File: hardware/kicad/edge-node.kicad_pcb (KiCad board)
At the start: 4 copper layers, 140 x 70 mm, 0 parts

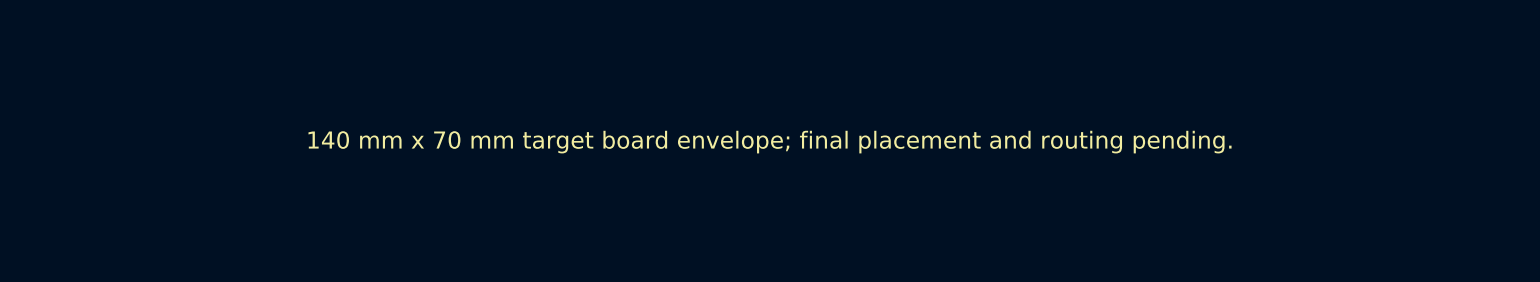
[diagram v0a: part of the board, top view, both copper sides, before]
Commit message: Add smartphone-first prototype and hosted backend
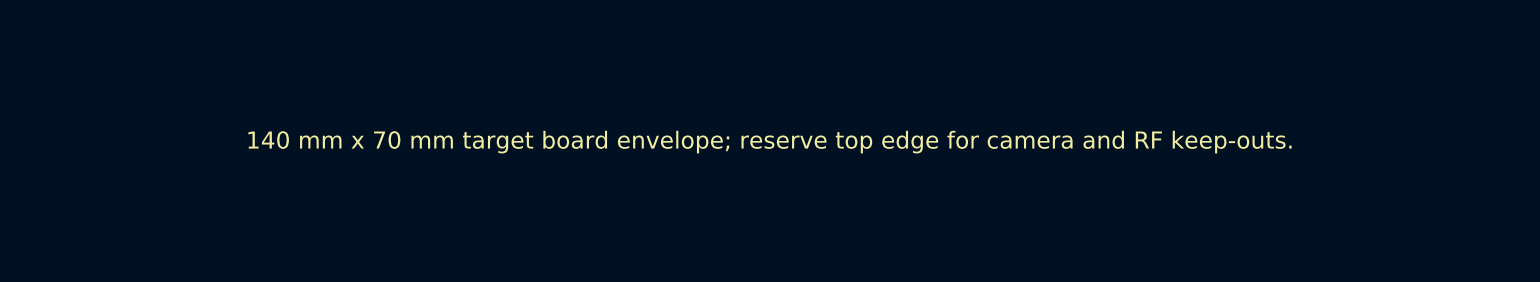
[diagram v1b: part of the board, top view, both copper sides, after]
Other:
- board text added: "140 mm x 70 mm target board envelope; reserve top edge for camera and RF keep-outs."
- board text removed: "140 mm x 70 mm target board envelope; final placement and routing pending."
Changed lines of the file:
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@@
   )
   (gr_rect (start 0 0) (end 140 70) (stroke (width 0.1) (type default)) (fill none) (layer "Edge.Cuts"))
-  (gr_text "140 mm x 70 mm target board envelope; final placement and routing pending." (at 70 35 0) (layer "F.SilkS"))
+  (gr_text "140 mm x 70 mm target board envelope; reserve top edge for camera and RF keep-outs." (at 70 35 0) (layer "F.SilkS"))
 )
